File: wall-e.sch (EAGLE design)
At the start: 69 parts, among them IC1 VREG-TS1117CW-3V3, T1 BC847, U1 TSM2306CX, U2 TSM2306CX, U3 TSM2306CX, U4 TSM2306CX, U5 TSM2306CX, U6 TSM2306CX, U7 TSM2306CX, U8 LM293AD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

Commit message: Last corrections on the schematic
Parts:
- added C15: 100nF, rcl:C-EUC0805
- added R1: 2.2k, rcl:R-US_R0805
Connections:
- removed net DEBUG_LED: LED1.A, U$1.PC13
- new net N$11: R1.1, U$1.PC13
- new net N$18: LED1.A, R1.2
- net GND: now also C15.2
- net MCU_RESET: now also C15.1
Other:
- moved on the sheet: LED1
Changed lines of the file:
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@@
 <part name="GND13" library="supply1" deviceset="GND" device=""/>
 <part name="GND29" library="supply1" deviceset="GND" device=""/>
+<part name="C15" library="rcl" deviceset="C-EU" device="C0805" value="100nF"/>
+<part name="GND20" library="supply1" deviceset="GND" device=""/>
+<part name="R1" library="rcl" deviceset="R-US_" device="R0805" value="2.2k"/>
 </parts>
 <sheets>
@@
 <instance part="P+14" gate="1" x="243.84" y="-40.64"/>
 <instance part="P+20" gate="1" x="294.64" y="-40.64"/>
-<instance part="LED1" gate="G$1" x="33.02" y="91.44" rot="R270"/>
-<instance part="GND28" gate="1" x="25.4" y="86.36"/>
+<instance part="LED1" gate="G$1" x="20.32" y="91.44" rot="R270"/>
+<instance part="GND28" gate="1" x="12.7" y="86.36"/>
 <instance part="C3" gate="G$1" x="22.86" y="58.42"/>
 <instance part="+3V16" gate="G$1" x="254" y="149.86"/>
@@
 <instance part="GND13" gate="1" x="147.32" y="139.7"/>
 <instance part="GND29" gate="1" x="182.88" y="139.7"/>
+<instance part="C15" gate="G$1" x="-2.54" y="63.5"/>
+<instance part="GND20" gate="1" x="-2.54" y="53.34"/>
+<instance part="R1" gate="G$1" x="30.48" y="91.44" rot="R180"/>
 </instances>
 <busses>
@@
 </segment>
 <segment>
-<pinref part="LED1" gate="G$1" pin="C"/>
-<wire x1="27.94" y1="91.44" x2="25.4" y2="91.44" width="0.1524" layer="91"/>
-<wire x1="25.4" y1="91.44" x2="25.4" y2="88.9" width="0.1524" layer="91"/>
-<pinref part="GND28" gate="1" pin="GND"/>
-</segment>
-<segment>
 <wire x1="22.86" y1="213.36" x2="25.4" y2="213.36" width="0.1524" layer="91"/>
 <wire x1="25.4" y1="213.36" x2="25.4" y2="210.82" width="0.1524" layer="91"/>
@@
 <wire x1="185.42" y1="144.78" x2="182.88" y2="144.78" width="0.1524" layer="91"/>
 <wire x1="182.88" y1="144.78" x2="182.88" y2="142.24" width="0.1524" layer="91"/>
+</segment>
+<segment>
+<pinref part="C15" gate="G$1" pin="2"/>
+<wire x1="-2.54" y1="58.42" x2="-2.54" y2="55.88" width="0.1524" layer="91"/>
+<pinref part="GND20" gate="1" pin="GND"/>
+</segment>
+<segment>
+<pinref part="LED1" gate="G$1" pin="C"/>
+<pinref part="GND28" gate="1" pin="GND"/>
+<wire x1="15.24" y1="91.44" x2="12.7" y2="91.44" width="0.1524" layer="91"/>
+<wire x1="12.7" y1="91.44" x2="12.7" y2="88.9" width="0.1524" layer="91"/>
 </segment>
 </net>
@@
 <pinref part="R19" gate="G$1" pin="1"/>
 <junction x="33.02" y="68.58"/>
-<wire x1="33.02" y1="68.58" x2="30.48" y2="68.58" width="0.1524" layer="91"/>
-<label x="12.7" y="68.58" size="1.778" layer="95"/>
+<label x="5.08" y="71.12" size="1.778" layer="95"/>
+<wire x1="33.02" y1="68.58" x2="-2.54" y2="68.58" width="0.1524" layer="91"/>
+<wire x1="-2.54" y1="68.58" x2="-2.54" y2="66.04" width="0.1524" layer="91"/>
+<pinref part="C15" gate="G$1" pin="1"/>
 </segment>
 <segment>
@@
 </segment>
 </net>
-<net name="DEBUG_LED" class="0">
-<segment>
-<pinref part="U$1" gate="G$1" pin="PC13"/>
-<wire x1="38.1" y1="91.44" x2="35.56" y2="91.44" width="0.1524" layer="91"/>
-<pinref part="LED1" gate="G$1" pin="A"/>
-</segment>
-</net>
 <net name="MOTOR1_1" class="0">
 <segment>
@@
 </segment>
 </net>
+<net name="N$11" class="0">
+<segment>
+<pinref part="U$1" gate="G$1" pin="PC13"/>
+<pinref part="R1" gate="G$1" pin="1"/>
+<wire x1="38.1" y1="91.44" x2="35.56" y2="91.44" width="0.1524" layer="91"/>
+</segment>
+</net>
+<net name="N$18" class="0">
+<segment>
+<pinref part="R1" gate="G$1" pin="2"/>
+<pinref part="LED1" gate="G$1" pin="A"/>
+<wire x1="25.4" y1="91.44" x2="22.86" y2="91.44" width="0.1524" layer="91"/>
+</segment>
+</net>

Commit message: Placement
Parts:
- removed ON/OFF: SWITCH, switch:SWITCH
- added C16: 100nF, rcl:C-EUC0805
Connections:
- removed net N$30: BATT-1.SK, ON/OFF.3
- net +12V: now also BATT-1.SK; no longer ON/OFF.1, ON/OFF.2
- net +3V3: no longer U8.VCC
- net +5V: now also C16.2, U8.VCC
- net GND: now also C16.1
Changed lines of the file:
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@@
 <part name="AX12" library="con-molex-spox" deviceset="5267-3" device=""/>
 <part name="AX12-2" library="con-molex-spox" deviceset="5267-3" device=""/>
-<part name="ON/OFF" library="switch" deviceset="SWITCH" device=""/>
 <part name="P+13" library="supply1" deviceset="+12V" device=""/>
 <part name="P+15" library="supply1" deviceset="+12V" device=""/>
@@
 <part name="R17" library="resistor" deviceset="R-US_" device="R0805" value="2.2K"/>
 <part name="+3V14" library="supply1" deviceset="+3V3" device=""/>
-<part name="+3V15" library="supply1" deviceset="+3V3" device=""/>
 <part name="SV4" library="con-lstb" deviceset="MA03-1" device=""/>
 <part name="SV5" library="con-lstb" deviceset="MA03-1" device=""/>
@@
 <part name="GND20" library="supply1" deviceset="GND" device=""/>
 <part name="R1" library="rcl" deviceset="R-US_" device="R0805" value="2.2k"/>
+<part name="P+18" library="supply1" deviceset="+5V" device=""/>
+<part name="C16" library="rcl" deviceset="C-EU" device="C0805" value="100nF"/>
+<part name="GND24" library="supply1" deviceset="GND" device=""/>
 </parts>
 <sheets>
@@
 <instance part="AX12" gate="G$1" x="314.96" y="144.78"/>
 <instance part="AX12-2" gate="G$1" x="314.96" y="162.56"/>
-<instance part="ON/OFF" gate="G$1" x="-121.92" y="96.52" rot="R270"/>
 <instance part="P+13" gate="1" x="-129.54" y="40.64"/>
 <instance part="P+15" gate="1" x="-119.38" y="106.68"/>
@@
 <instance part="P+16" gate="1" x="309.88" y="170.18"/>
 <instance part="GND10" gate="1" x="134.62" y="45.72"/>
-<instance part="P+10" gate="1" x="-45.72" y="45.72"/>
+<instance part="P+10" gate="1" x="-45.72" y="48.26"/>
 <instance part="U$3" gate="G$1" x="147.32" y="-45.72"/>
 <instance part="C4" gate="G$1" x="38.1" y="-25.4"/>
@@
 <instance part="R17" gate="G$1" x="292.1" y="114.3" rot="R270"/>
 <instance part="+3V14" gate="G$1" x="292.1" y="121.92"/>
-<instance part="+3V15" gate="G$1" x="-101.6" y="33.02"/>
 <instance part="SV4" gate="G$1" x="266.7" y="-45.72" rot="R180"/>
 <instance part="SV5" gate="G$1" x="317.5" y="-45.72" rot="R180"/>
@@
 <instance part="GND20" gate="1" x="-2.54" y="53.34"/>
 <instance part="R1" gate="G$1" x="30.48" y="91.44" rot="R180"/>
+<instance part="P+18" gate="1" x="-101.6" y="40.64"/>
+<instance part="C16" gate="G$1" x="-106.68" y="35.56" rot="R90"/>
+<instance part="GND24" gate="1" x="-109.22" y="30.48"/>
 </instances>
 <busses>
@@
 <wire x1="12.7" y1="91.44" x2="12.7" y2="88.9" width="0.1524" layer="91"/>
 </segment>
+<segment>
+<pinref part="C16" gate="G$1" pin="1"/>
+<pinref part="GND24" gate="1" pin="GND"/>
+<wire x1="-109.22" y1="35.56" x2="-109.22" y2="33.02" width="0.1524" layer="91"/>
+</segment>
 </net>
 <net name="+5V" class="0">
@@
 <pinref part="LD1" gate="G$1" pin="A"/>
 <wire x1="-48.26" y1="25.4" x2="-45.72" y2="25.4" width="0.1524" layer="91"/>
-<wire x1="-45.72" y1="25.4" x2="-45.72" y2="40.64" width="0.1524" layer="91"/>
+<wire x1="-45.72" y1="25.4" x2="-45.72" y2="43.18" width="0.1524" layer="91"/>
+<pinref part="P+10" gate="1" pin="+5V"/>
 <pinref part="R11" gate="G$1" pin="2"/>
-<wire x1="-114.3" y1="40.64" x2="-45.72" y2="40.64" width="0.1524" layer="91"/>
-<wire x1="-45.72" y1="40.64" x2="-45.72" y2="43.18" width="0.1524" layer="91"/>
-<junction x="-45.72" y="40.64"/>
-<pinref part="P+10" gate="1" pin="+5V"/>
+<wire x1="-45.72" y1="43.18" x2="-45.72" y2="45.72" width="0.1524" layer="91"/>
+<wire x1="-114.3" y1="40.64" x2="-114.3" y2="43.18" width="0.1524" layer="91"/>
+<wire x1="-114.3" y1="43.18" x2="-45.72" y2="43.18" width="0.1524" layer="91"/>
+<junction x="-45.72" y="43.18"/>
 </segment>
 <segment>
@@
 <wire x1="185.42" y1="157.48" x2="182.88" y2="157.48" width="0.1524" layer="91"/>
 <wire x1="182.88" y1="157.48" x2="182.88" y2="160.02" width="0.1524" layer="91"/>
+</segment>
+<segment>
+<pinref part="U8" gate="A" pin="VCC"/>
+<wire x1="-99.06" y1="27.94" x2="-101.6" y2="27.94" width="0.1524" layer="91"/>
+<wire x1="-101.6" y1="27.94" x2="-101.6" y2="35.56" width="0.1524" layer="91"/>
+<pinref part="P+18" gate="1" pin="+5V"/>
+<pinref part="C16" gate="G$1" pin="2"/>
+<wire x1="-101.6" y1="35.56" x2="-101.6" y2="38.1" width="0.1524" layer="91"/>
+<junction x="-101.6" y="35.56"/>
 </segment>
 </net>
@@
 </segment>
 <segment>
-<pinref part="U8" gate="A" pin="VCC"/>
-<wire x1="-99.06" y1="27.94" x2="-101.6" y2="27.94" width="0.1524" layer="91"/>
-<wire x1="-101.6" y1="27.94" x2="-101.6" y2="30.48" width="0.1524" layer="91"/>
-<pinref part="+3V15" gate="G$1" pin="+3V3"/>
-</segment>
-<segment>
 <pinref part="C3" gate="G$1" pin="2"/>
 <wire x1="15.24" y1="53.34" x2="22.86" y2="53.34" width="0.1524" layer="91"/>
@@
 </segment>
 <segment>
-<pinref part="ON/OFF" gate="G$1" pin="1"/>
-<wire x1="-127" y1="99.06" x2="-127" y2="101.6" width="0.1524" layer="91"/>
-<pinref part="ON/OFF" gate="G$1" pin="2"/>
-<wire x1="-127" y1="101.6" x2="-119.38" y2="101.6" width="0.1524" layer="91"/>
-<wire x1="-119.38" y1="101.6" x2="-119.38" y2="96.52" width="0.1524" layer="91"/>
+<wire x1="-119.38" y1="104.14" x2="-119.38" y2="96.52" width="0.1524" layer="91"/>
 <pinref part="C9" gate="G$1" pin="+"/>
 <pinref part="U$2" gate="G$1" pin="VI"/>
@@
 <wire x1="-104.14" y1="96.52" x2="-104.14" y2="99.06" width="0.1524" layer="91"/>
 <wire x1="-119.38" y1="96.52" x2="-114.3" y2="96.52" width="0.1524" layer="91"/>
+<junction x="-114.3" y="96.52"/>
+<pinref part="P+15" gate="1" pin="+12V"/>
+<pinref part="BATT" gate="-1" pin="SK"/>
+<wire x1="-132.08" y1="96.52" x2="-119.38" y2="96.52" width="0.1524" layer="91"/>
 <junction x="-119.38" y="96.52"/>
-<junction x="-114.3" y="96.52"/>
-<wire x1="-119.38" y1="104.14" x2="-119.38" y2="101.6" width="0.1524" layer="91"/>
-<junction x="-119.38" y="101.6"/>
-<pinref part="P+15" gate="1" pin="+12V"/>
 </segment>
 <segment>
@@
 <pinref part="R11" gate="G$1" pin="1"/>
 <wire x1="-114.3" y1="27.94" x2="-114.3" y2="30.48" width="0.1524" layer="91"/>
-<wire x1="-114.3" y1="27.94" x2="-106.68" y2="27.94" width="0.1524" layer="91"/>
-<wire x1="-106.68" y1="27.94" x2="-106.68" y2="20.32" width="0.1524" layer="91"/>
+<wire x1="-114.3" y1="27.94" x2="-109.22" y2="27.94" width="0.1524" layer="91"/>
+<wire x1="-109.22" y1="27.94" x2="-109.22" y2="20.32" width="0.1524" layer="91"/>
 <junction x="-114.3" y="27.94"/>
 <pinref part="U8" gate="A" pin="1IN-"/>
-<wire x1="-106.68" y1="20.32" x2="-99.06" y2="20.32" width="0.1524" layer="91"/>
+<wire x1="-109.22" y1="20.32" x2="-99.06" y2="20.32" width="0.1524" layer="91"/>
 </segment>
 </net>
@@
 </segment>
 </net>
-<net name="N$30" class="0">
-<segment>
-<pinref part="BATT" gate="-1" pin="SK"/>
-<pinref part="ON/OFF" gate="G$1" pin="3"/>
-<wire x1="-132.08" y1="96.52" x2="-127" y2="96.52" width="0.1524" layer="91"/>
-<wire x1="-127" y1="96.52" x2="-127" y2="93.98" width="0.1524" layer="91"/>
-</segment>
-</net>

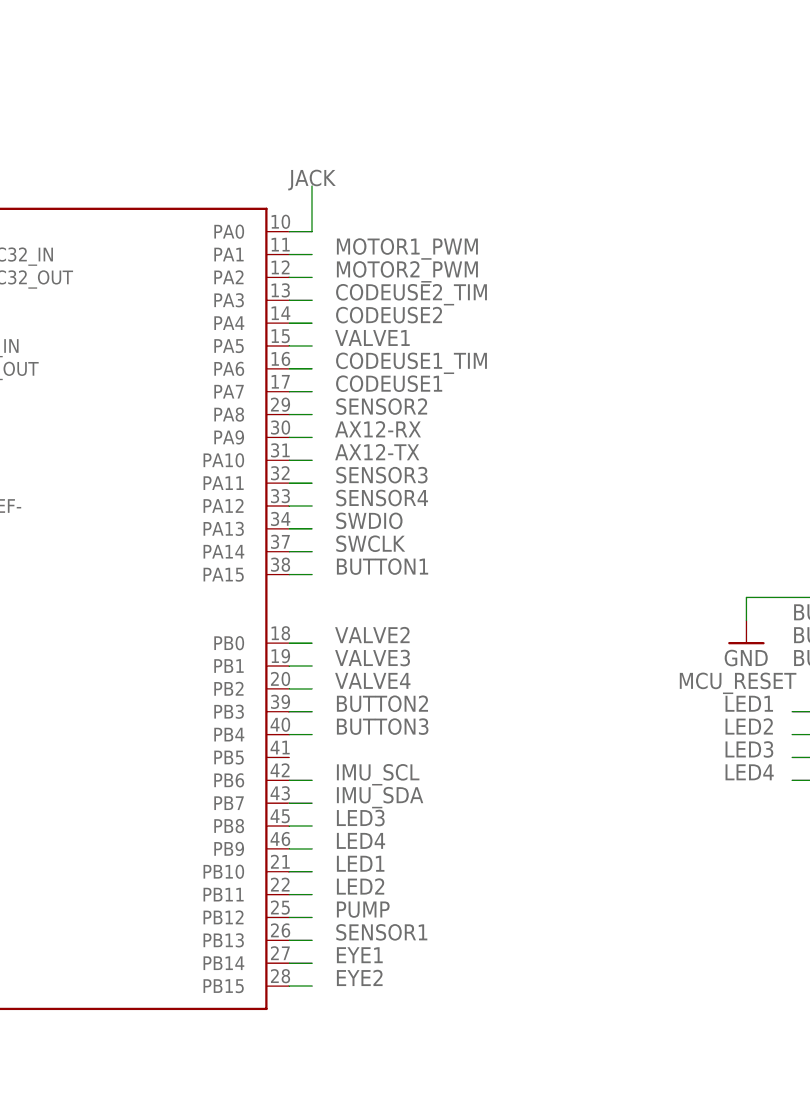
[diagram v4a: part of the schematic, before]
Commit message: Better allocation of the pins
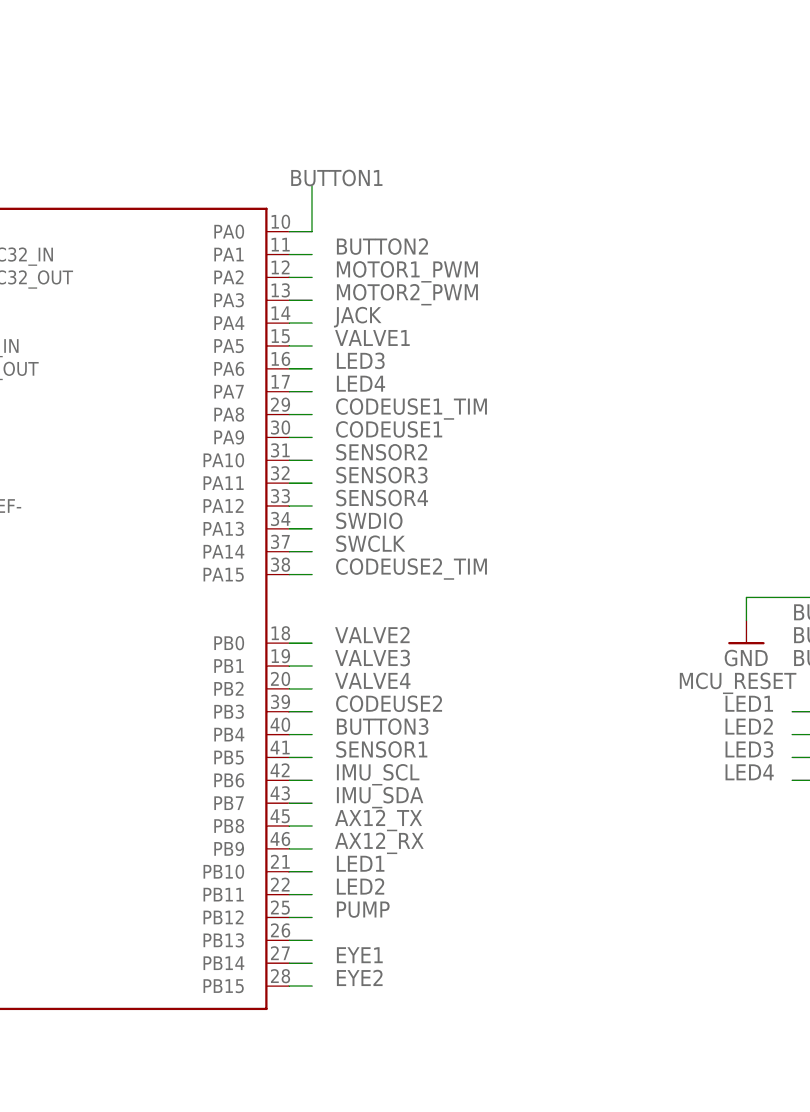
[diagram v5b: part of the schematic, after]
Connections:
- new net AX12_RX: U$1.PB9
- new net AX12_TX: U$1.PB8
- new net N$22: U$1.PB13
- net AX12-RX: no longer U$1.PA9
- net AX12-TX: no longer U$1.PA10
- net BUTTON1: now also U$1.PA0; no longer U$1.PA15
- net BUTTON2: now also U$1.PA1; no longer U$1.PB3
- net CODEUSE1: now also U$1.PA9; no longer U$1.PA7
- net CODEUSE1_TIM: now also U$1.PA8; no longer U$1.PA6
- net CODEUSE2: now also U$1.PB3; no longer U$1.PA4
- net CODEUSE2_TIM: now also U$1.PA15; no longer U$1.PA3
- net JACK: now also U$1.PA4; no longer U$1.PA0
- net LED3: now also U$1.PA6; no longer U$1.PB8
- net LED4: now also U$1.PA7; no longer U$1.PB9
- net MOTOR1_PWM: now also U$1.PA2; no longer U$1.PA1
- net MOTOR2_PWM: now also U$1.PA3; no longer U$1.PA2
- net SENSOR1: now also U$1.PB5; no longer U$1.PB13
- net SENSOR2: now also U$1.PA10; no longer U$1.PA8

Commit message: Routing
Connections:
- net LED1: now also R5.1, U$1.PB11; no longer R4.1, U$1.PB10
- net LED2: now also R3.1, U$1.PA7; no longer R2.1, U$1.PB11
- net LED3: now also R4.1; no longer R3.1
- net LED4: now also R2.1, U$1.PB10; no longer R5.1, U$1.PA7
- net SENSOR3: now also X1-5.1; no longer X1-4.1
- net SENSOR4: now also X1-4.1; no longer X1-5.1
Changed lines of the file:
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@@
 <net name="LED1" class="0">
+<segment>
+<pinref part="U$1" gate="G$1" pin="PB11"/>
+<wire x1="83.82" y1="17.78" x2="86.36" y2="17.78" width="0.1524" layer="91"/>
+<label x="88.9" y="17.78" size="1.778" layer="95"/>
+</segment>
+<segment>
+<pinref part="R5" gate="G$1" pin="1"/>
+<wire x1="142.24" y1="30.48" x2="139.7" y2="30.48" width="0.1524" layer="91"/>
+<label x="132.08" y="30.48" size="1.778" layer="95"/>
+</segment>
+</net>
+<net name="LED2" class="0">
+<segment>
+<pinref part="U$1" gate="G$1" pin="PA7"/>
+<wire x1="83.82" y1="73.66" x2="86.36" y2="73.66" width="0.1524" layer="91"/>
+<label x="88.9" y="73.66" size="1.778" layer="95"/>
+</segment>
+<segment>
+<pinref part="R3" gate="G$1" pin="1"/>
+<wire x1="142.24" y1="33.02" x2="139.7" y2="33.02" width="0.1524" layer="91"/>
+<label x="132.08" y="33.02" size="1.778" layer="95"/>
+</segment>
+</net>
+<net name="LED3" class="0">
+<segment>
+<pinref part="U$1" gate="G$1" pin="PA6"/>
+<wire x1="83.82" y1="76.2" x2="86.36" y2="76.2" width="0.1524" layer="91"/>
+<label x="88.9" y="76.2" size="1.778" layer="95"/>
+</segment>
 <segment>
 <pinref part="R4" gate="G$1" pin="1"/>
@@
 <label x="132.08" y="38.1" size="1.778" layer="95"/>
 </segment>
+</net>
+<net name="LED4" class="0">
 <segment>
 <pinref part="U$1" gate="G$1" pin="PB10"/>
@@
 <label x="88.9" y="20.32" size="1.778" layer="95"/>
 </segment>
-</net>
-<net name="LED2" class="0">
 <segment>
 <pinref part="R2" gate="G$1" pin="1"/>
 <wire x1="142.24" y1="35.56" x2="139.7" y2="35.56" width="0.1524" layer="91"/>
 <label x="132.08" y="35.56" size="1.778" layer="95"/>
-</segment>
-<segment>
-<pinref part="U$1" gate="G$1" pin="PB11"/>
-<wire x1="83.82" y1="17.78" x2="86.36" y2="17.78" width="0.1524" layer="91"/>
-<label x="88.9" y="17.78" size="1.778" layer="95"/>
-</segment>
-</net>
-<net name="LED3" class="0">
-<segment>
-<pinref part="R3" gate="G$1" pin="1"/>
-<wire x1="142.24" y1="33.02" x2="139.7" y2="33.02" width="0.1524" layer="91"/>
-<label x="132.08" y="33.02" size="1.778" layer="95"/>
-</segment>
-<segment>
-<pinref part="U$1" gate="G$1" pin="PA6"/>
-<wire x1="83.82" y1="76.2" x2="86.36" y2="76.2" width="0.1524" layer="91"/>
-<label x="88.9" y="76.2" size="1.778" layer="95"/>
-</segment>
-</net>
-<net name="LED4" class="0">
-<segment>
-<pinref part="R5" gate="G$1" pin="1"/>
-<wire x1="142.24" y1="30.48" x2="139.7" y2="30.48" width="0.1524" layer="91"/>
-<label x="132.08" y="30.48" size="1.778" layer="95"/>
-</segment>
-<segment>
-<pinref part="U$1" gate="G$1" pin="PA7"/>
-<wire x1="83.82" y1="73.66" x2="86.36" y2="73.66" width="0.1524" layer="91"/>
-<label x="88.9" y="73.66" size="1.778" layer="95"/>
 </segment>
 </net>
@@
 <net name="SENSOR3" class="0">
 <segment>
-<pinref part="X1" gate="-4" pin="1"/>
-<wire x1="157.48" y1="81.28" x2="154.94" y2="81.28" width="0.1524" layer="91"/>
-<label x="142.24" y="81.28" size="1.778" layer="95"/>
-</segment>
-<segment>
 <pinref part="U$1" gate="G$1" pin="PA11"/>
 <wire x1="83.82" y1="63.5" x2="86.36" y2="63.5" width="0.1524" layer="91"/>
 <label x="88.9" y="63.5" size="1.778" layer="95"/>
 </segment>
-</net>
-<net name="SENSOR4" class="0">
 <segment>
 <pinref part="X1" gate="-5" pin="1"/>
@@
 <label x="142.24" y="78.74" size="1.778" layer="95"/>
 </segment>
+</net>
+<net name="SENSOR4" class="0">
 <segment>
 <pinref part="U$1" gate="G$1" pin="PA12"/>
@@
 <label x="88.9" y="60.96" size="1.778" layer="95"/>
 </segment>
+<segment>
+<pinref part="X1" gate="-4" pin="1"/>
+<wire x1="157.48" y1="81.28" x2="154.94" y2="81.28" width="0.1524" layer="91"/>
+<label x="142.24" y="81.28" size="1.778" layer="95"/>
+</segment>
 </net>
